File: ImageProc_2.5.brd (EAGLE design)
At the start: 45.7 x 20.3 mm, 50 parts, among them J2 MOLEX_5034800600, U1 MIC5335-SPYMT, U11 ANTENNA-CHIP, U2 MIC5320-JGYML, U3 AT45DB321D, U4 ITG-3200, U6 ECS-2033, U7 ECS-160-8, U8 AT86RF231-ZU, U9 MN13822-L

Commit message: Stopped commiting for a week. Oops.
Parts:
- removed BALUN1: HHM1710D1, stan:BALUN
- removed J2: MOLEX_5034800600, stan:MOLEX_5034800600
- removed LED4: Yellow, led:CHIP-LED0603
- removed LED5: Green, led:CHIP-LED0603
- removed LED6: Red, led:CHIP-LED0603
- removed PROC1: DSPIC33FJ128MC706A, stan:TQFP64
- removed U1: MIC5335-SPYMT, stan:MLF-6
- removed U11: ANTENNA-CHIP, stan:ANTENNA-CHIP
- removed U2: MIC5320-JGYML, stan:MLF-6
- removed U3: AT45DB321D, stan:MLF(VDFN)-8
- removed U4: ITG-3200, stan:QFN-24
- removed U6: ECS-2033, stan:OSCILLATOR-SMD
- removed U7: ECS-160-8, stan:CRYSTAL-SMD
- removed U8: AT86RF231-ZU, stan:QFN-32
- removed U9: MN13822-L, stan:SOT-23-3
- added ANT1: ANT8030-2R4-01A, biomimetic:ANT8030-2R4-01A
- added B1: HHM1710D1, biomimetic:0603-BALUN
- added C10, C20, C22, C27, C36, C37, C39, C40, C9: 0.1uF, biomimetic:0402-CAP
- added C18, C19: 10pF, biomimetic:0402-CAP
- added C21: 1uF, biomimetic:0402-CAP
- added C32, C35: 2.2uF, biomimetic:0402-CAP
- added C33: 22uF, biomimetic:0603-CAP
- added C34: 10nF, biomimetic:0402-CAP
- added C38: 2.2nF, biomimetic:0402-CAP
- added IC1: XC61GC3002HR-G, biomimetic:USP-3
- added IC10: AT45DB642D-CNU, biomimetic:CASON-8
- added IC2: MIC5335-SPYMT, biomimetic:MLF-6
- added IC3: MIC5335-JGYMT, biomimetic:MLF-6
- added IC4: DSPIC33FJ128MC706A, biomimetic:TQFP-64
- added IC5: AT86RF233-ZU, biomimetic:VQFN-32QN2
- added IC6: LTC6088, biomimetic:DFN-16
- added IC7, IC8: DRV8833RTY, biomimetic:S-PWQFN-N16
- added IC9: MPU-6000, biomimetic:QFN-24
- added JP1: MOLEX_503480-0600, biomimetic:MOLEX_503480-0600
- added JP4: 51441-2493-C, biomimetic:MOLEX_52740-2490
- added L1: 4.7uH, biomimetic:0603
- added LED1: YELLOW, biomimetic:LED-0603
- added LED2, LED_RX: GREEN, biomimetic:LED-0603
- added LED3, LED_TX: RED, biomimetic:LED-0603
- added OSC1: ECS-2033-400, biomimetic:OSCILLATOR-SMD
- added OSC2: NX2520SA-16.000000MHZ, biomimetic:CRYSTAL-SMD
- added P1: BAT+, wirepad:SMD1,27-2,54
- added P10: MD2, wirepad:SMD1,27-2,54
- added P11: EXT1, wirepad:SMD1,27-2,54
- added P12: EXT2, wirepad:SMD1,27-2,54
- added P13: EXT3, wirepad:SMD1,27-2,54
- added P14: EXT4, wirepad:SMD1,27-2,54
- added P15: EXT5, wirepad:SMD1,27-2,54
- added P16: EXT6, wirepad:SMD1,27-2,54
- added P2: BAT-, wirepad:SMD1,27-2,54
- added P3: MA1, wirepad:SMD1,27-2,54
- added P4: MA2, wirepad:SMD1,27-2,54
- added P5: MB1, wirepad:SMD1,27-2,54
- added P6: MB2, wirepad:SMD1,27-2,54
- added P7: MC1, wirepad:SMD1,27-2,54
- added P8: MC2, wirepad:SMD1,27-2,54
- added P9: MD1, wirepad:SMD1,27-2,54
- added R12, R15, R21, R22, R25, R8: 15k, biomimetic:0402-RES
- added R14, R19, R20, R23, R24, R9: 47k, biomimetic:0402-RES
- added R26, R27, R28, R6, R7: 2.7k, biomimetic:0402-RES
- added R5: 4.7k, biomimetic:0402-RES
- C1: value 2.2nF -> 1uF; device SparkFun:0402-CAP -> biomimetic:0402-CAP
- C11, C12, C13, C24, C25, C26: value 1uF -> 0.1uF; device SparkFun:0402-CAP -> biomimetic:0402-CAP
- C14, C28: value 22pF -> 0.1uF; device SparkFun:0402-CAP -> biomimetic:0402-CAP
- C15: value 1uF -> 4.7uF; device SparkFun:0402-CAP -> biomimetic:0603-CAP
- C16, C17: value 1uF -> 22pF; device SparkFun:0402-CAP -> biomimetic:0402-CAP
- C2, C3, C31: device SparkFun:0402-CAP -> biomimetic:0402-CAP
- C23, C4, C5, C7: value 0.1uF -> 1uF; device SparkFun:0402-CAP -> biomimetic:0402-CAP
- C29: value 12pF -> 0.1uF; device SparkFun:0402-CAP -> biomimetic:0402-CAP
- C30: value 12pF -> 22uF; device SparkFun:0402-CAP -> biomimetic:0603-CAP
- C6: value 10nF -> 0.1uF; device SparkFun:0402-CAP -> biomimetic:0402-CAP
- C8: value 2.2uF -> 1uF; device SparkFun:0402-CAP -> biomimetic:0402-CAP
- JP2: value MPCS2PH -> MOLEX_503480-0600; device stan:MOLEX-PICO_CLASP_S2P -> biomimetic:MOLEX_503480-0600
- JP3: value 51441-2493-C -> MOLEX_503480-0600; device stan:MOLEX-52740-2490 -> biomimetic:MOLEX_503480-0600
- R1: value 4.7k -> 1k; device rcl:R0402 -> biomimetic:0402-RES
- R10: value 10k -> 47k; device rcl:R0402 -> biomimetic:0402-RES
- R11: value 470 -> 15k; device rcl:R0402 -> biomimetic:0402-RES
- R13: value 470 -> 47k; device rcl:R0402 -> biomimetic:0402-RES
- R16: value 27K -> 4.7k; device rcl:R0402 -> biomimetic:0402-RES
- R17: value 10K -> 15k; device rcl:R0402 -> biomimetic:0402-RES
- R18: value 470 -> 4.7k; device rcl:R0402 -> biomimetic:0402-RES
- R2: value 4.7k -> 2.7k; device rcl:R0402 -> biomimetic:0402-RES
- R3, R4: device rcl:R0402 -> biomimetic:0402-RES
- moved C8 129.4 mm to (13.6, 16.3), flipped to the bottom, turned to 270 degrees
- moved R10 129.2 mm to (-6.11, 19.9), flipped to the bottom
- moved R11 128.3 mm to (-6.16, 18.4), flipped to the bottom
- moved R13 126.6 mm to (-6.10, 15.9), flipped to the bottom, turned to 180 degrees
- moved R18 122.8 mm to (11.7, 13.7), flipped to the bottom, turned to 270 degrees
- moved R4 119.8 mm to (14.5, 10.4), flipped to the bottom, turned to 270 degrees
- moved R2 118.7 mm to (9.83, 16.1), flipped to the bottom, turned to 270 degrees
- moved R1 118.4 mm to (12.5, 16.2), flipped to the bottom, turned to 90 degrees
- moved R3 114.5 mm to (28.2, 12.4), flipped to the bottom
- moved C7 96.3 mm to (14.9, 16.1), flipped to the bottom, turned to 270 degrees
- moved C1 83.4 mm to (16.6, 18.6), flipped to the bottom, turned to 270 degrees
- moved C6 83.3 mm to (11.2, 16.2), flipped to the bottom, turned to 90 degrees
- moved C5 82.3 mm to (5.71, 18.7), flipped to the bottom
- moved C4 77.3 mm to (9.28, 13.7), flipped to the bottom, turned to 90 degrees
- moved C3 62.3 mm to (8.51, 16.2), flipped to the bottom, turned to 270 degrees
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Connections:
- removed net AN0: C31.2, PROC1.16, R16.2, R17.1
- removed net AN1: PROC1.15
- removed net AN10: PROC1.23
- removed net AN11: PROC1.24
- removed net AN3: PROC1.13
- removed net AN4: PROC1.12
- removed net AN5: PROC1.11
- removed net BAT+: C15.1, C24.1, JP2.1, R17.2, U1.1, U1.3, U1.4, U2.1, U2.3, U2.4, U9.2
- removed net INT1: PROC1.42, U4.12
- removed net INT2: PROC1.43, U9.1
- removed net INT3: PROC1.44
- removed net INT4: PROC1.45, U8.24
- removed net MCLR: J2.P5, PROC1.7, R10.1
- removed net OSC1: JP3.12, PROC1.39, U6.3
- removed net OSC2: PROC1.40
- removed net PWM1: PROC1.60
- removed net PWM1H: PROC1.61
- removed net PWM2: PROC1.62
- removed net PWM2H: PROC1.63
- removed net PWM3: PROC1.64
- removed net PWM3H: PROC1.1
- removed net PWM4: PROC1.2
- removed net PWM4H: PROC1.3
- removed net RB15: PROC1.30, U8.11
- removed net RC13: JP3.18, PROC1.47
- removed net RC14: JP3.17, PROC1.48
- removed net RD0: PROC1.46
- removed net RD1: PROC1.49
- removed net RD10: JP3.6
- removed net RD11: JP3.7
- removed net RD12: JP3.9
- removed net RD13: JP3.11
- removed net RD14: JP3.13
- removed net RD15: JP3.4
- removed net RD2: PROC1.50
- removed net RD3: PROC1.51
- removed net RD4: PROC1.52
- removed net RD5: PROC1.53
- removed net RD6: PROC1.54
- removed net RD7: PROC1.55
- removed net RD8: JP3.3
- removed net RD9: JP3.5
- removed net RF0: JP3.16, PROC1.58
- removed net RF1: JP3.8, PROC1.59
- removed net SCL2: PROC1.32, R4.1, U4.23
- removed net SDA2: PROC1.31, R3.1, U4.24
- removed net SS1: PROC1.14, U8.23
- removed net SS2: PROC1.8, U3.4
- removed net VCC: C17.1, C3.2, JP3.14, JP3.21, U2.6
- removed net VDD: C12.1, C2.1, C23.1, C25.1, C4.1, C6.1, C7.1, J2.P4, PROC1.10, PROC1.19, PROC1.26, PROC1.38, PROC1.57, R1.2, R10.2, R2.2, R3.2, R4.2, U1.6, U3.3, U3.5, U3.6, U4.13, U4.8, U6.4, U8.15, U8.28, U8.8
- removed net VEE: C16.1, JP3.15, U2.5
- removed net VPP: C26.1, U1.5
- new net !RESET: IC10.3, IC4.7, IC5.8, JP1.1, R3.1
- new net !SS1: IC4.14, IC5.23
- new net !SS2_1: IC10.4, IC4.8
- new net !SS2_2: IC4.40, IC9.8
- new net 1.8V: C8.1, IC3.5, JP4.15
- new net 2.5V: C2.1, C36.2, IC3.6, JP4.14, JP4.21
- new net 3.0V: C7.1, IC2.5
- new net 3.3V: C1.1, C11.1, C12.1, C13.1, C14.1, C21.1, C23.1, C37.1, C40.1, C9.1, IC10.5, IC10.6, IC2.6, IC4.10, IC4.26, IC4.38, IC4.57, IC5.15, IC5.28, IC9.13, JP1.2, JP3.1, L1.2, OSC1.4, R3.2, R4.2, R5.2
- new net 40MHZ: IC4.39, JP4.12, OSC1.3
- new net BATT_LEVEL: C6.1, IC4.16, R1.1, R2.2
- new net CAM_D0: IC4.46, JP4.6
- new net CAM_D1: IC4.49, JP4.4
- new net CAM_D2: IC4.50, JP4.3
- new net CAM_D3: IC4.51, JP4.5
- new net CAM_D4: IC4.52, JP4.7
- new net CAM_D5: IC4.53, JP4.9
- new net CAM_D6: IC4.54, JP4.11
- new net CAM_D7: IC4.55, JP4.13
- new net CAM_HREF: IC4.58, IC9.11, JP4.16
- new net CAM_PCLK: IC4.59, JP4.8
- new net CAM_PWDN: IC4.48, JP4.17
- new net CAM_VSYNC: IC4.47, JP4.18
- new net EXT1: IC4.15, P11.1
- new net EXT2: IC4.13, P12.1
- new net EXT3: IC4.12, P13.1
- new net EXT4: IC4.11, P14.1
- new net EXT5: IC4.42, P15.1
- new net EXT6: IC4.44, P16.1
- new net GN_LED: IC4.28, LED2.A
- new net LOWBATT_IRQ: IC1.2, IC4.43
- new net MOTOR_A_BEMF: IC4.21, IC6.1, R8.2
- new net MOTOR_A_IN1: IC4.61, IC7.14
- new net MOTOR_A_IN2: IC4.60, IC7.13
- new net MOTOR_A_OUT1: C24.1, IC7.16, P3.1, R9.1
- new net MOTOR_A_OUT2: C24.2, IC7.2, P4.1, R10.1
- new net MOTOR_B_BEMF: IC4.22, IC6.7, R12.2
- new net MOTOR_B_IN1: IC4.63, IC7.7
- new net MOTOR_B_IN2: IC4.62, IC7.8
- new net MOTOR_B_OUT1: C25.1, IC7.5, P5.1, R13.1
- new net MOTOR_B_OUT2: C25.2, IC7.3, P6.1, R14.1
- new net MOTOR_C_BEMF: IC4.23, IC6.10, R17.2
- new net MOTOR_C_IN1: IC4.1, IC8.14
- new net MOTOR_C_IN2: IC4.64, IC8.13
- new net MOTOR_C_OUT1: C27.1, IC8.16, P7.1, R19.1
- new net MOTOR_C_OUT2: C27.2, IC8.2, P8.1, R20.1
- new net MOTOR_D_BEMF: IC4.24, IC6.16, R22.2
- new net MOTOR_D_IN1: IC4.3, IC8.7
- new net MOTOR_D_IN2: IC4.2, IC8.8
- new net MOTOR_D_OUT1: C28.1, IC8.5, P9.1, R23.1
- new net MOTOR_D_OUT2: C28.2, IC8.3, P10.1, R24.1
- new net N$1: C22.2, IC5.13, IC5.14
- new net N$11: LED_RX.C, R7.1
- new net N$21: C10.1, IC4.19, L1.1
- new net N$24: IC6.11, R17.1, R19.2
- new net N$3: C20.2, IC5.29
- new net N$31: IC6.3, R10.2, R11.2
- new net N$32: C39.2, IC9.10
- new net N$6: C16.1, IC5.4
- new net N$7: C17.2, IC5.5
- new net N$8: C19.1, IC5.25, OSC2.3
- new net N$9: C18.1, IC5.26, OSC2.1
- new net PGC: IC4.17, JP1.5
- new net PGD: IC4.18, JP1.4
- new net RADIO_IRQ: IC4.45, IC5.24
- new net RADIO_SLP_TR: IC4.30, IC5.11
- new net RD_LED: IC4.27, LED3.A
- new net U2RX: IC4.31, JP2.6
- new net U2TX: IC4.32, JP2.4
- new net V_BATT: C29.1, C3.1, C30.1, C31.1, C33.1, C34.1, C4.2, C5.2, IC1.3, IC2.1, IC2.3, IC2.4, IC3.1, IC3.3, IC3.4, IC6.4, IC7.10, IC7.15, IC8.10, IC8.15, JP2.1, JP2.2, P1.1, R1.2, R16.2
- new net V_REF: C26.1, R11.1, R15.1, R16.1, R18.2, R21.1, R25.1
- new net YW_LED: IC4.29, LED1.A
- net GND: now also B1.2, B1.5, C1.2, C10.2, C14.2, C18.2, C19.2, C20.1, C21.2, C22.1, C3.2, C32.2, C33.2, C35.2, C36.1, C37.2, C38.1, C39.1, C4.1, C40.2, C5.1, C9.2, IC1.1, IC10.7, IC2.2, IC2.EPAD, IC3.2, IC3.EPAD, IC4.20, IC4.25, IC4.41, IC4.9, IC5.12, IC5.16, IC5.18, IC5.21, IC5.27, IC5.3, IC5.30, IC5.31, IC5.32, IC5.6, IC5.7, IC5.PAD, IC6.13, IC6.PAD, IC7.1, IC7.11, IC7.4, IC7.PPAD, IC8.1, IC8.11, IC8.4, IC8.PPAD, IC9.1, IC9.18, JP1.3, JP2.3, JP2.5, JP3.2, JP3.4, JP3.6, JP4.10, JP4.19, JP4.23, OSC1.2, OSC2.2, OSC2.4, P2.1, R18.1, R2.1, R26.2, R27.2, R28.2, R6.2, R7.2; no longer BALUN1.2, BALUN1.5, BALUN1.6, C1.1, C16.2, C17.2, C24.2, C25.2, C3.1, C31.1, C4.2, C5.2, J2.P3, JP2.2, JP3.10, JP3.19, JP3.23, PROC1.20, PROC1.25, PROC1.41, PROC1.9, R11.2, R13.2, R16.1, R18.2, U1.2, U2.2, U3.7, U4.1, U4.11, U4.18, U4.9, U6.2, U7.2, U7.4, U8.12, U8.16, U8.18, U8.21, U8.27, U8.3, U8.30, U8.31, U8.32, U8.6, U8.7, U8.P$1, U9.3
- net N$10: now also B1.3, C17.1; no longer BALUN1.4, C14.1
- net N$12: now also B1.4, C16.2; no longer BALUN1.3, C28.1
- net N$13: now also IC5.1, LED_RX.A; no longer C14.2, U8.4
- net N$14: now also IC5.10, LED_TX.A; no longer C28.2, U8.5
- net N$15: now also LED1.C, R26.1; no longer BALUN1.1, U11.SIG
- net N$16: now also LED2.C, R27.1; no longer C30.1, U7.3, U8.25
- net N$17: now also LED3.C, R28.1; no longer C29.1, U7.1, U8.26
- net N$18: now also C32.1, IC7.12; no longer C1.2, U4.20
- net N$19: now also C34.2, IC8.9; no longer C5.1, U4.10
- net N$2: now also C31.2, IC7.9; no longer J2.P6, PROC1.21
- net N$20: now also C35.1, IC8.12; no longer LED4.C, R11.1
- net N$22: now also IC6.6, R12.1, R13.2; no longer LED4.A, PROC1.29
- net N$23: now also IC6.5, R14.2, R15.2; no longer J2.P1, PROC1.17
- net N$25: now also IC6.12, R20.2, R21.2; no longer J2.P2, PROC1.18
- net N$26: now also IC6.15, R22.1, R23.2; no longer LED5.C, R13.1
- net N$27: now also IC6.14, R24.2, R25.2; no longer LED6.C, R18.1
- net N$28: now also C15.1, IC4.56; no longer LED5.A, PROC1.28
- net N$29: now also C38.2, IC9.20; no longer LED6.A, PROC1.27
- net N$30: now also IC6.2, R8.1, R9.2; no longer C8.1, PROC1.56
- net N$4: now also ANT1.A, B1.1; no longer C11.1, U8.29
- net N$5: now also LED_TX.C, R6.1; no longer C13.1, U8.13, U8.14
- net SCK1: now also IC4.35, IC5.19; no longer PROC1.35, U8.19
- net SCK2: now also IC10.2, IC4.4, IC9.23; no longer PROC1.4, U3.2
- net SCL1: now also IC4.36, JP3.3, JP4.20, R4.1; no longer JP3.20, PROC1.37, R1.1
- net SDA1: now also IC4.37, JP3.5, JP4.22, R5.1; no longer JP3.22, PROC1.36, R2.1
- net SDI1: now also IC4.34, IC5.20; no longer PROC1.34, U8.20
- net SDI2: now also IC10.8, IC4.5, IC9.9; no longer PROC1.5, U3.8
- net SDO1: now also IC4.33, IC5.22; no longer PROC1.33, U8.22
- net SDO2: now also IC10.1, IC4.6, IC9.24; no longer PROC1.6, U3.1
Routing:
- added copper zone on layer 3, net 3.3V
- added copper zone on layer 1, net GND
- added copper zone on layer 16, net GND
- added copper zone on layer 2, net GND
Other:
- board text removed: "GYRO"
- board text removed: "I2C1"
- board text removed: "I2C2"
- board text removed: "ImageProc 2.4"
- board text removed: "LED"
- board text removed: "RADIO"
- board text removed: "UC Berkeley"
- board text removed: "WII"
- board text removed: "XL"

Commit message: Before work 6/30
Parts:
- moved C9 9.69 mm to (20.2, 7.11), turned to 0 degrees
- moved LED3 9.45 mm to (27.7, 9.91), turned to 90 degrees
- moved LED1 9.37 mm to (27.7, 11.0), turned to 90 degrees
- moved LED2 9.19 mm to (27.7, 12.3), turned to 90 degrees
- moved R3 8.86 mm to (19.5, 13.9), turned to 270 degrees
- moved R28 7.80 mm to (27.8, 9.91)
- moved R26 7.58 mm to (27.8, 11.0)
- moved R27 7.23 mm to (27.6, 12.3)
- moved C14 6.07 mm to (21.8, 7.77), turned to 0 degrees
- moved LED_RX 4.71 mm to (27.7, 6.10)
- moved LED_TX 4.54 mm to (27.7, 7.37)
- moved R7 3.28 mm to (27.7, 6.10), turned to 180 degrees
- moved R6 3.18 mm to (27.7, 7.37), turned to 180 degrees
- moved JP3 0.89 mm to (23.0, 17.7)
- moved JP1 0.70 mm to (27.7, 2.55)
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
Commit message: Work 6/30
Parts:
- moved OSC2 0.74 mm to (32.0, 11.1), turned to 90 degrees
- moved C16 0.33 mm to (34.9, 5.44)
- moved IC5 0.31 mm to (36.5, 9.60)
- moved B1 0.29 mm to (36.5, 5.28)
- moved C17 0.28 mm to (38.1, 5.44)
- moved ANT1 0.08 mm to (35.9, 2.41)
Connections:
- net 3.3V: now also C29.1, IC6.4
- net V_BATT: no longer C29.1, IC6.4

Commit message: Commit before replace LTC6088 with LT1991
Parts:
- added C41, C42, C44: (no value), biomimetic:0402-CAP
- added C43: xnF, biomimetic:0402-CAP
- added R29, R30, R31, R32: (no value), biomimetic:0402-RES
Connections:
- new net N$34: IC6.16, R22.2, R32.1
- new net N$35: IC6.10, R17.2, R31.1
- new net N$36: IC6.1, R29.1, R8.2
- new net N$37: IC6.7, R12.2, R30.1
- net GND: now also C41.2, C42.2, C43.2, C44.2
- net MOTOR_A_BEMF: now also C41.1, R29.2; no longer IC6.1, R8.2
- net MOTOR_B_BEMF: now also C42.1, R30.2; no longer IC6.7, R12.2
- net MOTOR_C_BEMF: now also C43.1, R31.2; no longer IC6.10, R17.2
- net MOTOR_D_BEMF: now also C44.1, R32.2; no longer IC6.16, R22.2

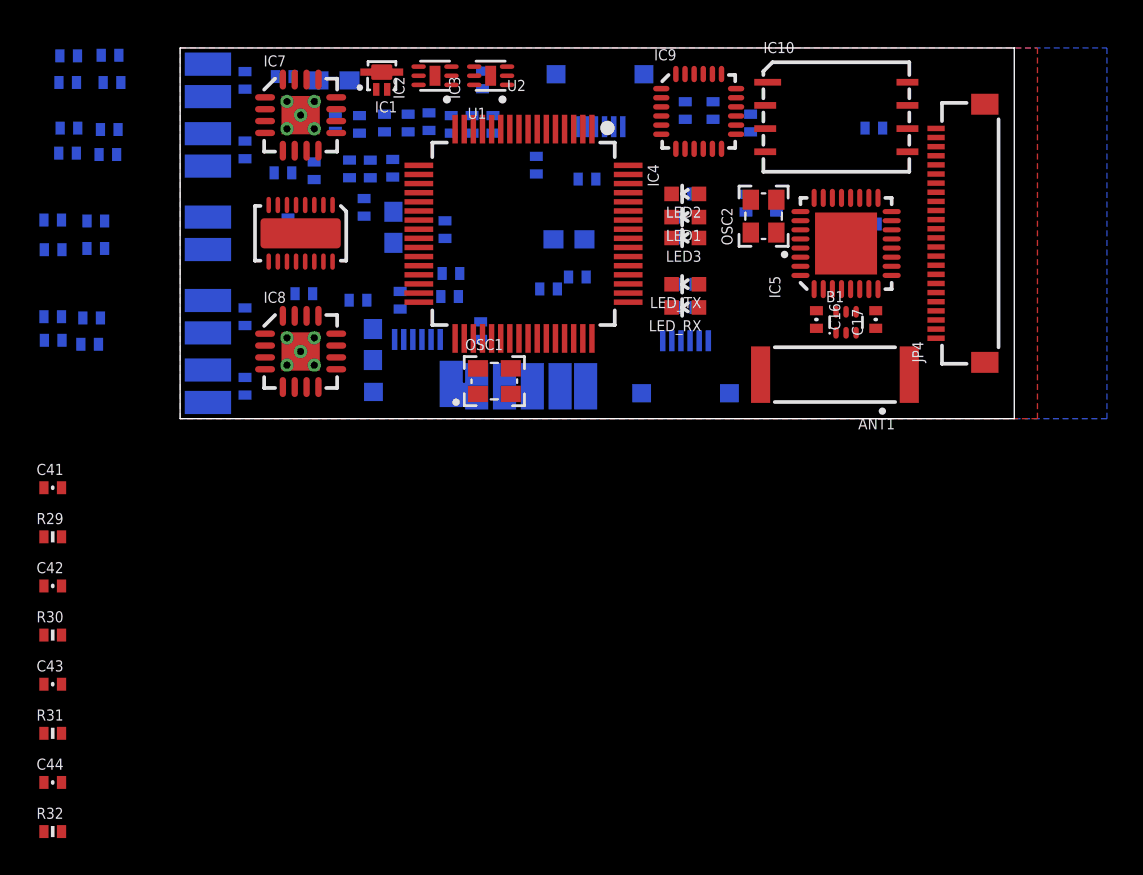
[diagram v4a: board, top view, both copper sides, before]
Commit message: Partial motor driver route. Motor drive vias moved to edge (could be used for strain relief).
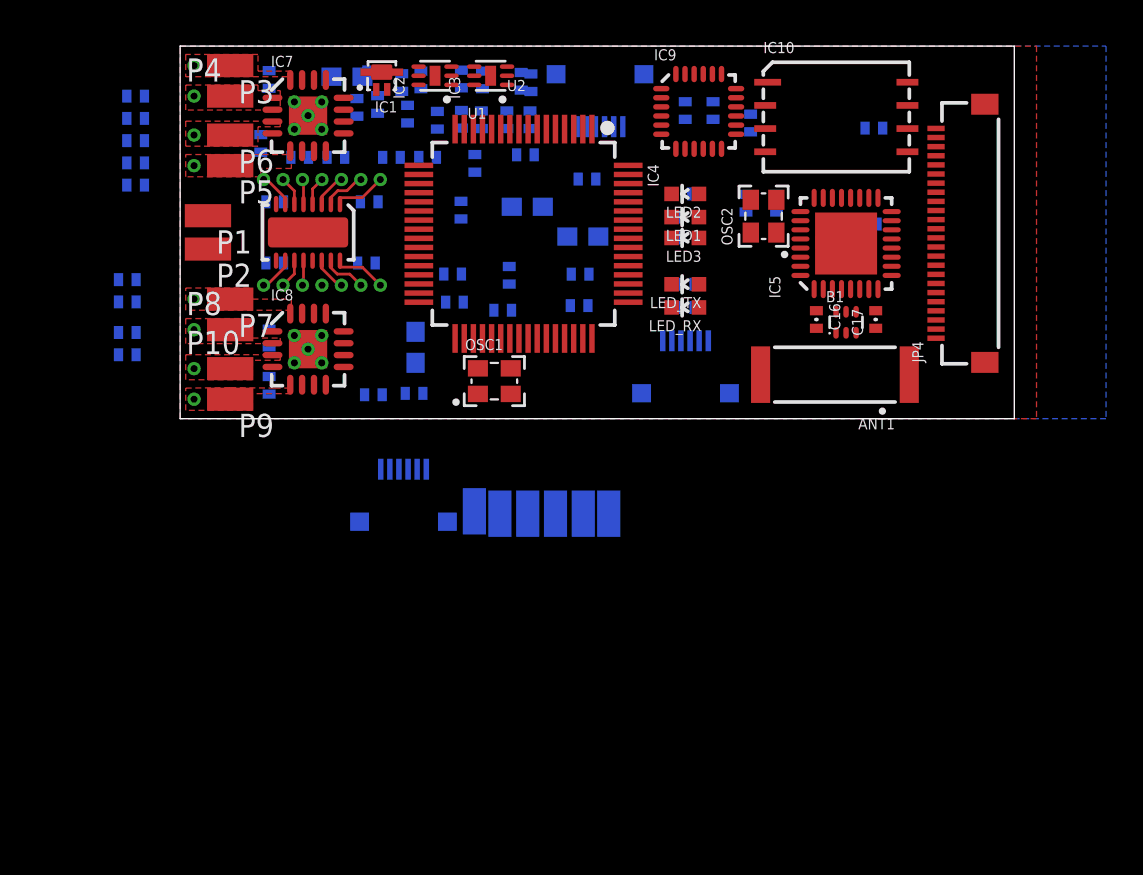
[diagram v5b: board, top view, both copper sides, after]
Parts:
- moved R30 29.5 mm to (6.55, 14.3), flipped to the bottom, turned to 180 degrees
- moved C42 28.2 mm to (8.53, 14.3), flipped to the bottom, turned to 180 degrees
- moved R29 27.9 mm to (11.6, 14.3), flipped to the bottom, turned to 180 degrees
- moved C41 27.4 mm to (13.6, 14.3), flipped to the bottom, turned to 180 degrees
- moved R32 26.5 mm to (-2.90, 3.51), flipped to the bottom
- moved C44 25.0 mm to (-2.90, 4.72), flipped to the bottom, turned to 180 degrees
- moved R31 24.0 mm to (-2.90, 6.40), flipped to the bottom
- moved C43 22.5 mm to (-2.90, 7.62), flipped to the bottom, turned to 180 degrees
- moved R22 15.8 mm to (10.2, 8.53)
- moved R8 15.5 mm to (10.4, 11.9), turned to 180 degrees
- moved R18 14.1 mm to (-2.44, 14.0), turned to 0 degrees
- moved R20 11.0 mm to (2.29, 4.88)
- moved R25 10.0 mm to (-2.44, 15.2), turned to 180 degrees
- moved R17 9.84 mm to (5.18, 8.53), turned to 0 degrees
- moved R23 9.74 mm to (2.29, 1.22)
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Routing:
- net N$36: track 0.00 -> 2.98 mm, vias 0 -> 1
- net N$34: track 0.00 -> 2.98 mm, vias 0 -> 1
- net N$26: track 0.00 -> 2.43 mm, vias 0 -> 1
- net N$30: track 0.00 -> 2.42 mm, vias 0 -> 1
- net N$37: track 0.00 -> 1.94 mm, vias 0 -> 1
- net N$35: track 0.00 -> 1.94 mm, vias 0 -> 1
- net N$31: track 0.00 -> 1.88 mm, vias 0 -> 1
- net N$27: track 0.00 -> 1.88 mm, vias 0 -> 1
- net N$22: track 0.00 -> 1.60 mm, vias 0 -> 1
- net N$24: track 0.00 -> 1.60 mm, vias 0 -> 1
- net 3.3V: track 0.00 -> 1.56 mm, vias 0 -> 1
- net N$23: track 0.00 -> 1.37 mm, vias 0 -> 1
- net N$25: track 0.00 -> 1.37 mm, vias 0 -> 1
- added copper zone on layer 1, net MOTOR_A_OUT1
- added copper zone on layer 1, net MOTOR_A_OUT2
- added copper zone on layer 1, net MOTOR_B_OUT1
- added copper zone on layer 1, net MOTOR_B_OUT2
- added copper zone on layer 1, net MOTOR_C_OUT1
- added copper zone on layer 1, net MOTOR_C_OUT2
- added copper zone on layer 1, net MOTOR_D_OUT1
- added copper zone on layer 1, net MOTOR_D_OUT2
- added copper zone on layer 3, net V_BATT
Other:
- board size 45.7 x 20.3 mm -> 45.7 x 20.4 mm

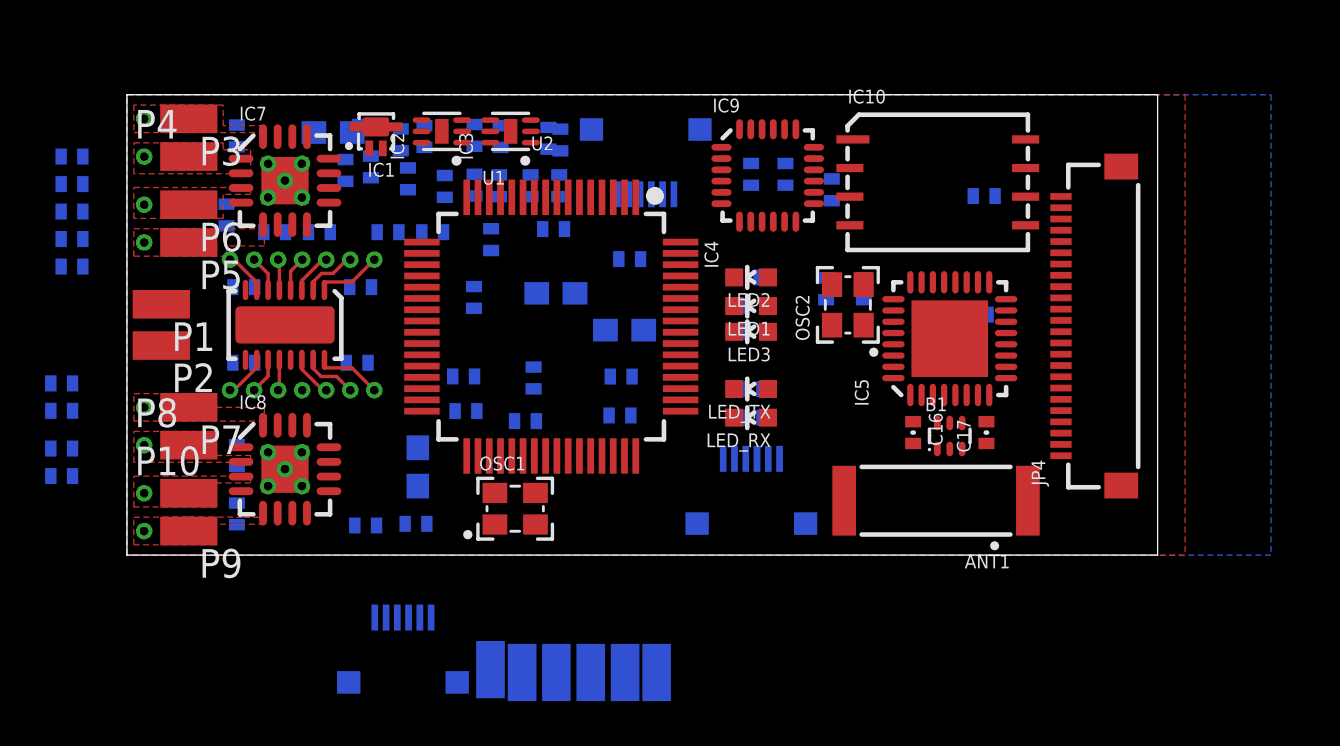
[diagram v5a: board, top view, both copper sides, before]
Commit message: Motor section mostly complete, except motor controller power and PIC analog pins. Camera connector escape complete. Edited PIC keepout to be tighter.
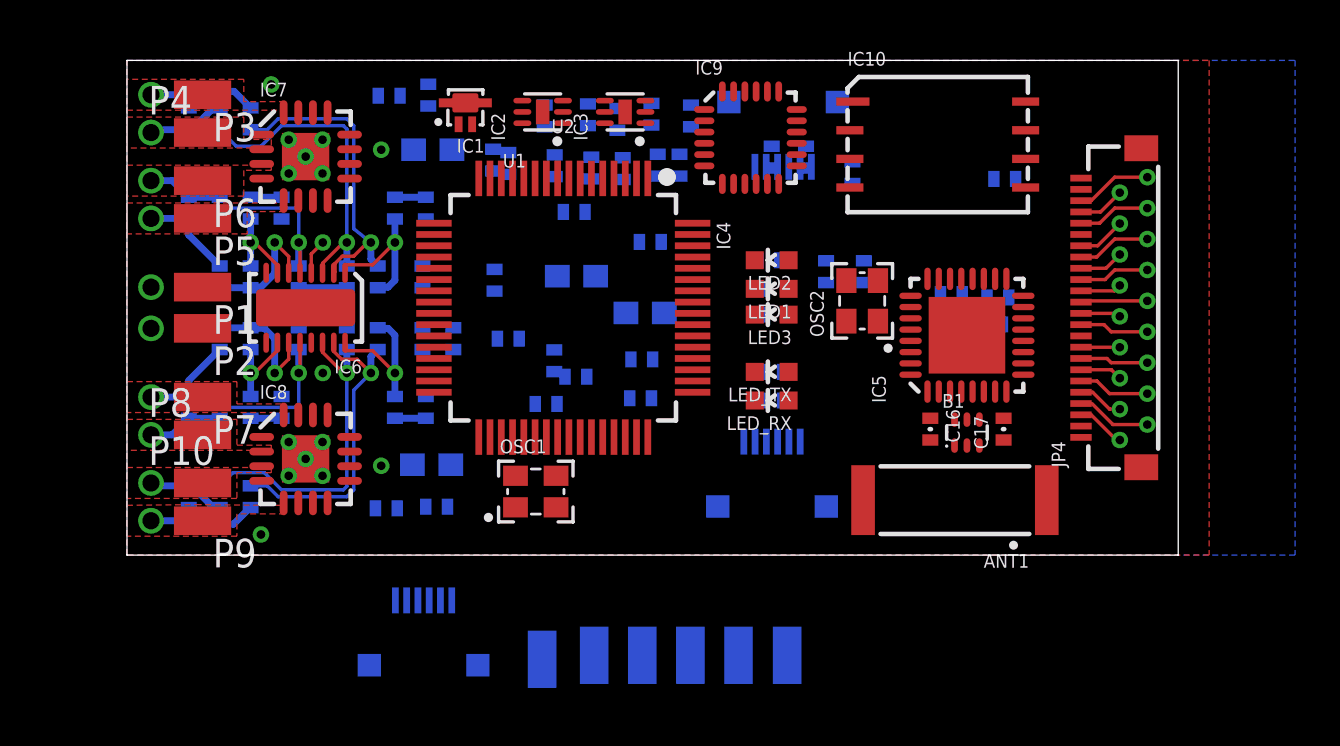
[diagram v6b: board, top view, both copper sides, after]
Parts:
- moved C44 16.3 mm to (13.3, 6.55), turned to 90 degrees
- moved R18 16.2 mm to (13.1, 9.60), turned to 90 degrees
- moved R32 15.1 mm to (11.9, 6.55), turned to 270 degrees
- moved R25 13.4 mm to (9.75, 9.60), turned to 270 degrees
- moved R11 13.3 mm to (9.75, 12.3), turned to 90 degrees
- moved R15 10.9 mm to (7.62, 12.3), turned to 90 degrees
- moved R21 10.6 mm to (7.62, 9.60), turned to 270 degrees
- moved C43 9.81 mm to (6.86, 6.55), turned to 90 degrees
- moved R31 8.38 mm to (5.49, 6.55), turned to 270 degrees
- moved C31 6.57 mm to (16.2, 17.5)
- moved JP3 6.22 mm to (29.1, 18.9)
- moved C29 6.10 mm to (16.9, 17.4)
- moved R2 5.89 mm to (25.0, 19.5)
- moved P13 5.84 mm to (29.3, -4.45)
- moved C2 5.71 mm to (23.5, 17.3)
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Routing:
- net N$31: track 1.88 -> 14.3 mm
- net N$27: track 1.88 -> 14.2 mm
- net N$30: track 2.42 -> 14.0 mm
- net N$26: track 2.43 -> 14.0 mm
- net N$25: track 1.37 -> 7.74 mm
- net N$23: track 1.37 -> 7.74 mm
- net V_REF: track 0.00 -> 5.69 mm
- net MOTOR_A_OUT1: track 0.00 -> 5.27 mm
- net MOTOR_D_OUT1: track 0.00 -> 5.27 mm
- net MOTOR_B_OUT1: track 0.00 -> 4.52 mm
- net MOTOR_C_OUT1: track 0.00 -> 4.33 mm
- net N$24: track 1.60 -> 5.77 mm
- net N$22: track 1.60 -> 5.68 mm
- net 2.5V: track 0.00 -> 3.90 mm, vias 0 -> 2
- net MOTOR_D_OUT2: track 0.00 -> 3.65 mm
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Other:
- board size 45.7 x 20.4 mm -> 46.6 x 21.9 mm

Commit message: Partial antenna and RF route. Adjusted ground planes to avoid antenna and moved antenna to lower-right corner, moved OVCAM connector up to make room.
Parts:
- moved C39 4.82 mm to (32.6, 14.9)
- moved ANT1 4.42 mm to (41.1, 2.44), turned to 0 degrees
- moved C38 2.81 mm to (30.7, 14.9)
- moved JP4 2.44 mm to (44.2, 13.4)
- moved C33 1.72 mm to (14.8, 19.2), turned to 90 degrees
- moved C15 1.48 mm to (21.9, 11.7), turned to 270 degrees
- moved OSC2 1.45 mm to (32.2, 12.6)
- moved R27 1.32 mm to (29.0, 14.3), turned to 90 degrees
- moved C11 1.26 mm to (18.9, 5.49), turned to 90 degrees
- moved JP1 1.23 mm to (28.5, 2.09)
- moved C13 1.04 mm to (22.5, 14.7), turned to 270 degrees
- moved C22 1.02 mm to (38.9, 12.4), turned to 90 degrees
- moved JP3 0.91 mm to (29.1, 19.9)
- moved C21 0.91 mm to (36.6, 12.5), turned to 90 degrees
- moved R6 0.80 mm to (29.1, 8.79), turned to 90 degrees
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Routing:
- net N$4: track 0.00 -> 3.18 mm
- net N$7: track 0.00 -> 2.20 mm
- net N$6: track 0.00 -> 2.20 mm
- net N$12: track 0.00 -> 1.45 mm
- net N$10: track 0.00 -> 1.18 mm

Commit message: RF top layout complete
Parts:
- moved LED2 12.5 mm to (23.3, 1.80)
- moved LED1 10.1 mm to (26.6, 1.91)
- moved LED3 8.92 mm to (29.8, 1.83)
- moved LED_TX 8.24 mm to (33.8, 1.73)
- moved R6 7.28 mm to (31.5, 1.93)
- moved LED_RX 6.21 mm to (33.8, 3.43)
- moved R7 4.48 mm to (31.5, 3.15)
- moved OSC2 1.41 mm to (30.8, 12.3)
- moved IC5 1.03 mm to (36.6, 11.1)
- moved C17 0.81 mm to (38.1, 6.40)
- moved B1 0.77 mm to (36.6, 6.40)
- moved C16 0.62 mm to (35.1, 6.40)
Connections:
- net CAM_D5 renamed N#3
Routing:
- net 3.3V: track 1.56 -> 8.07 mm, vias 1 -> 3
- net N$8: track 0.00 -> 5.20 mm, vias 0 -> 1
- net N$3: track 0.00 -> 4.75 mm, vias 0 -> 1
- net N$9: track 0.00 -> 4.44 mm, vias 0 -> 1
- net !RESET: track 0.00 -> 2.30 mm, vias 0 -> 1
- net RADIO_SLP_TR: track 0.00 -> 1.63 mm, vias 0 -> 1
- net N$1: track 0.00 -> 1.58 mm, vias 0 -> 1
- net N$14: track 0.00 -> 1.50 mm, vias 0 -> 1
- net N$4: track 3.18 -> 3.79 mm
